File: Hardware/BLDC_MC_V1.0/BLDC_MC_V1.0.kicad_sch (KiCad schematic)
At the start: 0 parts

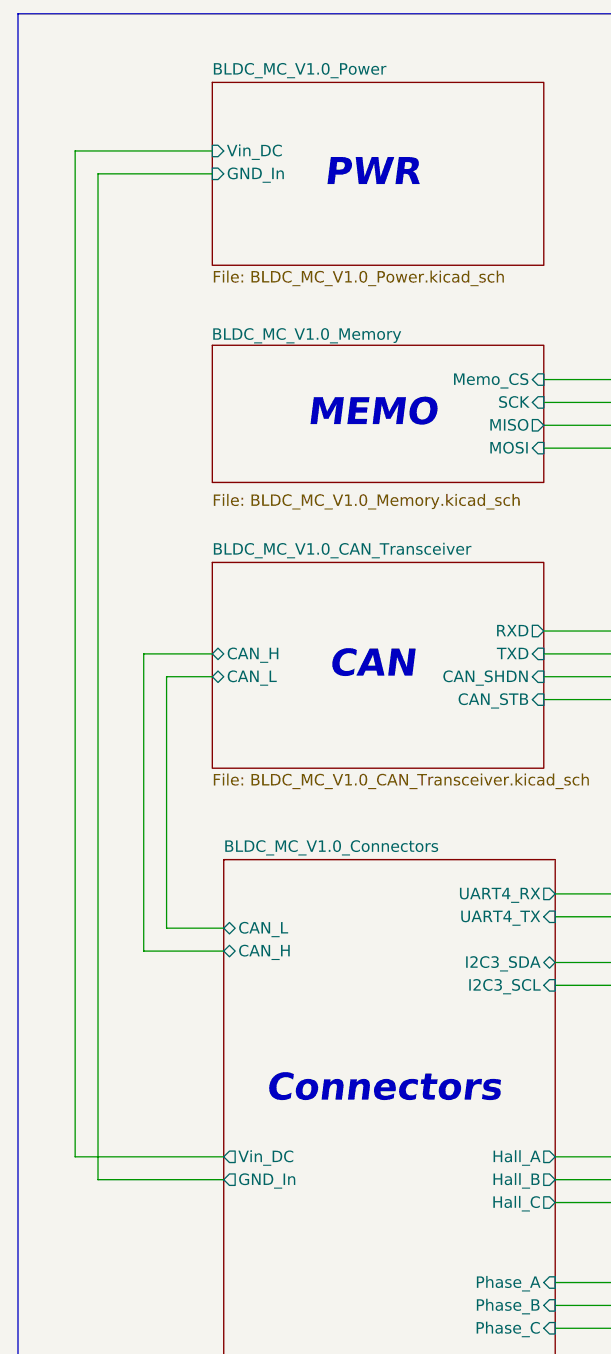
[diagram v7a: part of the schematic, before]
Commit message: Update the component placement of the board
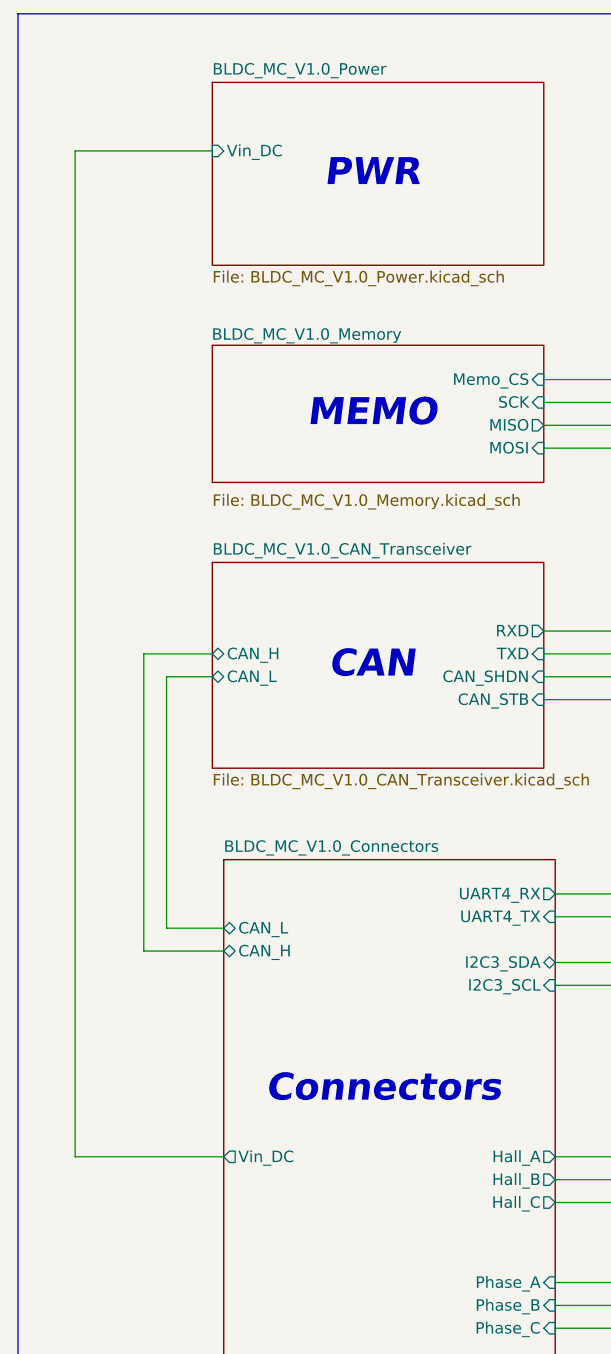
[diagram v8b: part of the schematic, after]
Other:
- sheet BLDC_MC_V1.0_Connectors ports: added none; removed GND_In
- sheet BLDC_MC_V1.0_Power ports: added none; removed GND_In
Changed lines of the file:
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@@
-	(wire
-		(pts
-			(xy 33.02 161.29) (xy 46.99 161.29)
-		)
-		(stroke
-			(width 0)
-			(type default)
-		)
-	)
 	(wire
 		(pts
@@
 	(wire
 		(pts
-			(xy 45.72 49.53) (xy 33.02 49.53)
-		)
-		(stroke
-			(width 0)
-			(type default)
-		)
-	)
-	(wire
-		(pts
 			(xy 82.55 77.47) (xy 92.71 77.47)
 		)
@@
 		(pts
 			(xy 208.28 53.34) (xy 228.6 53.34)
-		)
-		(stroke
-			(width 0)
-			(type default)
-		)
-	)
-	(wire
-		(pts
-			(xy 33.02 49.53) (xy 33.02 161.29)
 		)
 		(stroke
@@
 			)
 		)
-		(pin "GND_In" output
-			(at 46.99 161.29 180)
-			(effects
-				(font
-					(size 1.27 1.27)
-				)
-				(justify left)
-			)
-		)
 		(instances
 			(project "BLDC_MC_V1.0"
@@
 			)
 		)
-		(pin "GND_In" input
-			(at 45.72 49.53 180)
-			(effects
-				(font
-					(size 1.27 1.27)
-				)
-				(justify left)
-			)
-		)
